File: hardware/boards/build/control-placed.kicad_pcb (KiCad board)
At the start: 4 copper layers, 177.9 x 107.5 mm, 106 parts

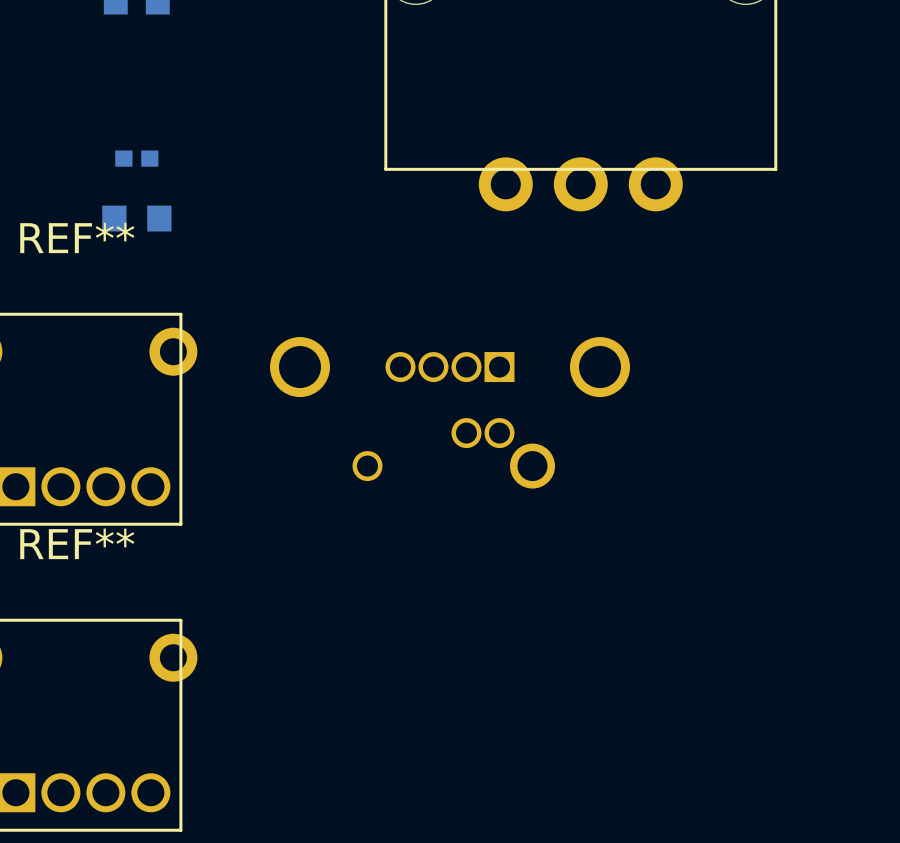
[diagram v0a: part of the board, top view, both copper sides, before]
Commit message: Move SD card slot from back to front of control board
The MicroSD slot needs to be accessible through the faceplate cutout,
so it must be on the front layer. Flipped footprint from B.Cu to F.Cu
in the KiCad PCB and added placement call in place_components.py to
position it at the faceplate cutout coordinates.

https://claude.ai/code/session_017d4oTDEiKrwHvNU6zuaWmu
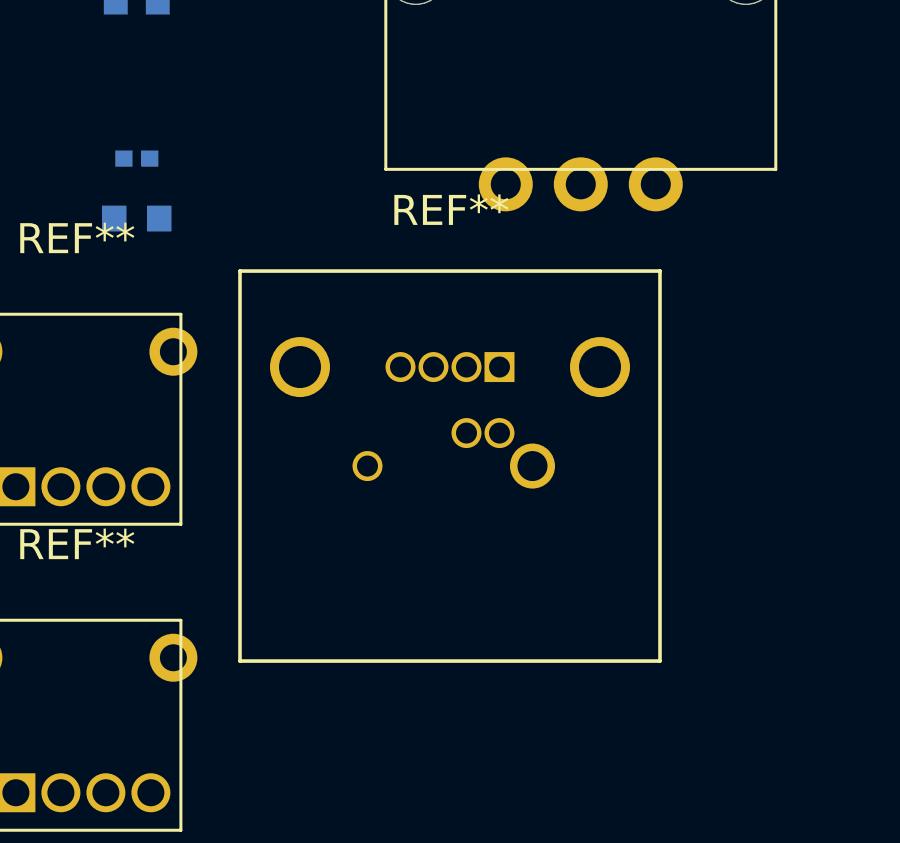
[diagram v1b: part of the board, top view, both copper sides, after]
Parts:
- REF**: moved to F.Cu
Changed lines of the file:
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@@
 	)
 	(footprint "PJS008U:PJS008U"
-		(layer "B.Cu")
+		(layer "F.Cu")
 		(at 100.94 90.25 180)
 		(property "Reference" "REF**"
 			(at 0 8.5 0)
-			(layer "B.SilkS")
+			(layer "F.SilkS")
 			(effects
 				(font
@@
 					(thickness 0.15)
 				)
-				(justify mirror)
 			)
 		)
 		(property "Value" "PJS008U"
 			(at 0 -8.5 0)
-			(layer "B.Fab")
+			(layer "F.Fab")
 			(effects
 				(font
@@
 					(thickness 0.15)
 				)
-				(justify mirror)
 			)
 		)
 		(property "Datasheet" ""
 			(at 0 0 0)
-			(layer "B.Fab")
+			(layer "F.Fab")
 			(hide yes)
 			(effects
@@
 					(thickness 0.15)
 				)
-				(justify mirror)
 			)
 		)
 		(property "Description" ""
 			(at 0 0 0)
-			(layer "B.Fab")
+			(layer "F.Fab")
 			(hide yes)
 			(effects
@@
 					(thickness 0.15)
 				)
-				(justify mirror)
 			)
 		)
@@
 				(type solid)
 			)
-			(layer "B.SilkS")
+			(layer "F.SilkS")
 		)
 		(fp_line
@@
 				(type solid)
 			)
-			(layer "B.SilkS")
+			(layer "F.SilkS")
 		)
 		(fp_line
@@
 				(type solid)
 			)
-			(layer "B.SilkS")
+			(layer "F.SilkS")
 		)
 		(fp_line
@@
 				(type solid)
 			)
-			(layer "B.SilkS")
+			(layer "F.SilkS")
 		)
 		(pad "" thru_hole circle

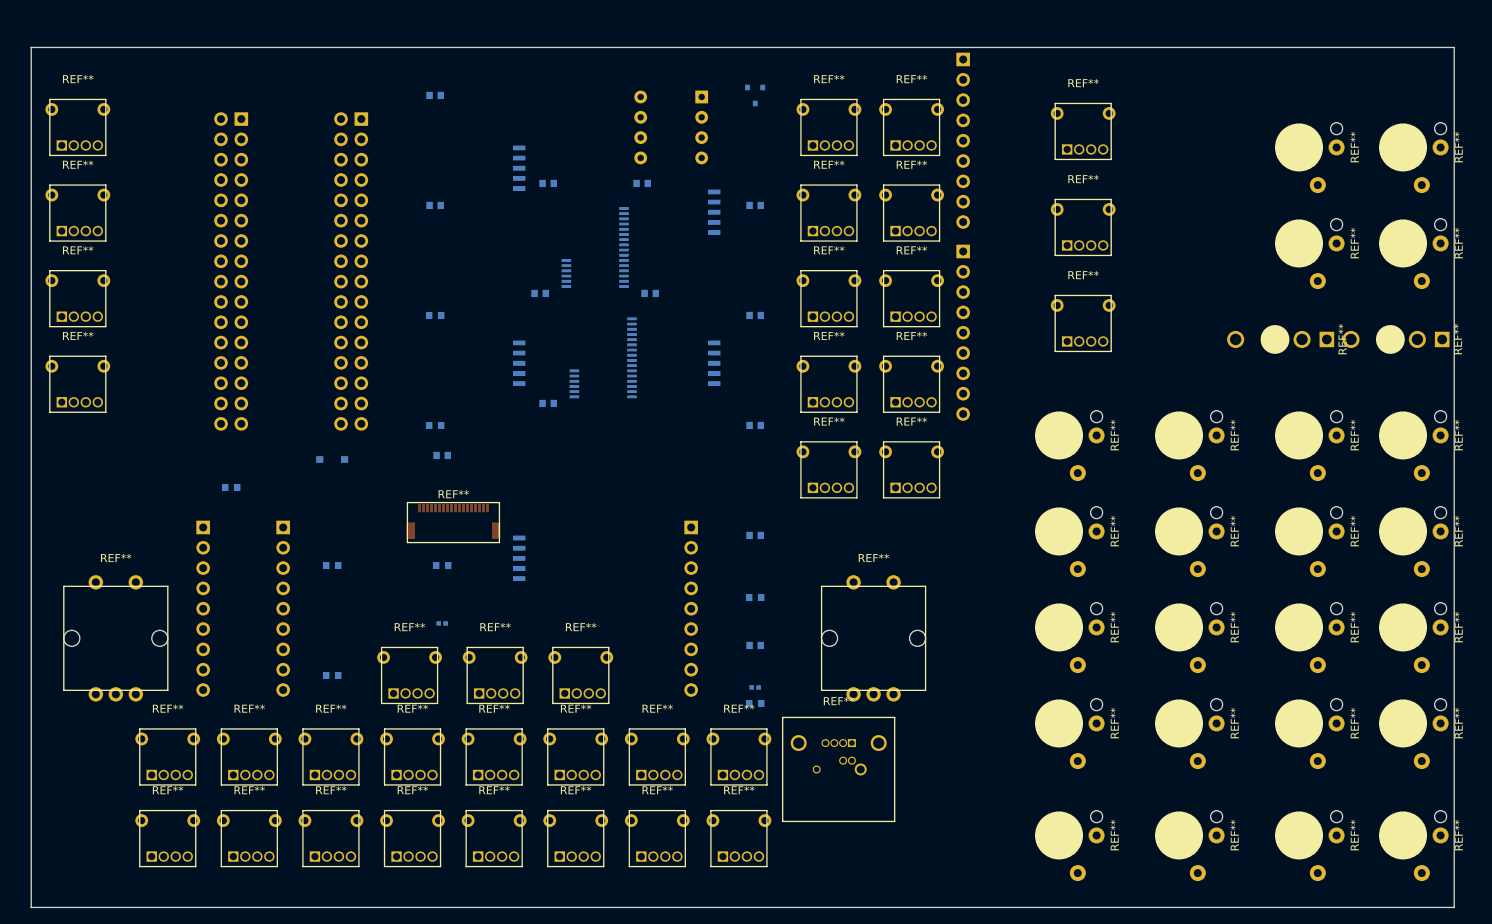
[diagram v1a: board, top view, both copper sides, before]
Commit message: Fix hardware pipeline: SD card position, faceplate holes, 3D assembly stack-up
- Fix SD card slot placement below PLAY button with component-map fallback
- Rebuild PJS008U 3D model as hollow card cage, align with faceplate cutout
- Inset USB-C connector flush with main board edge
- Add clock jack holes, SD cutout, JetBrains Mono fonts to faceplate
- Correct 3D assembly Z spacing from actual PJ398SM model measurements
- Improve explode animation: anchor control board, smoother slider
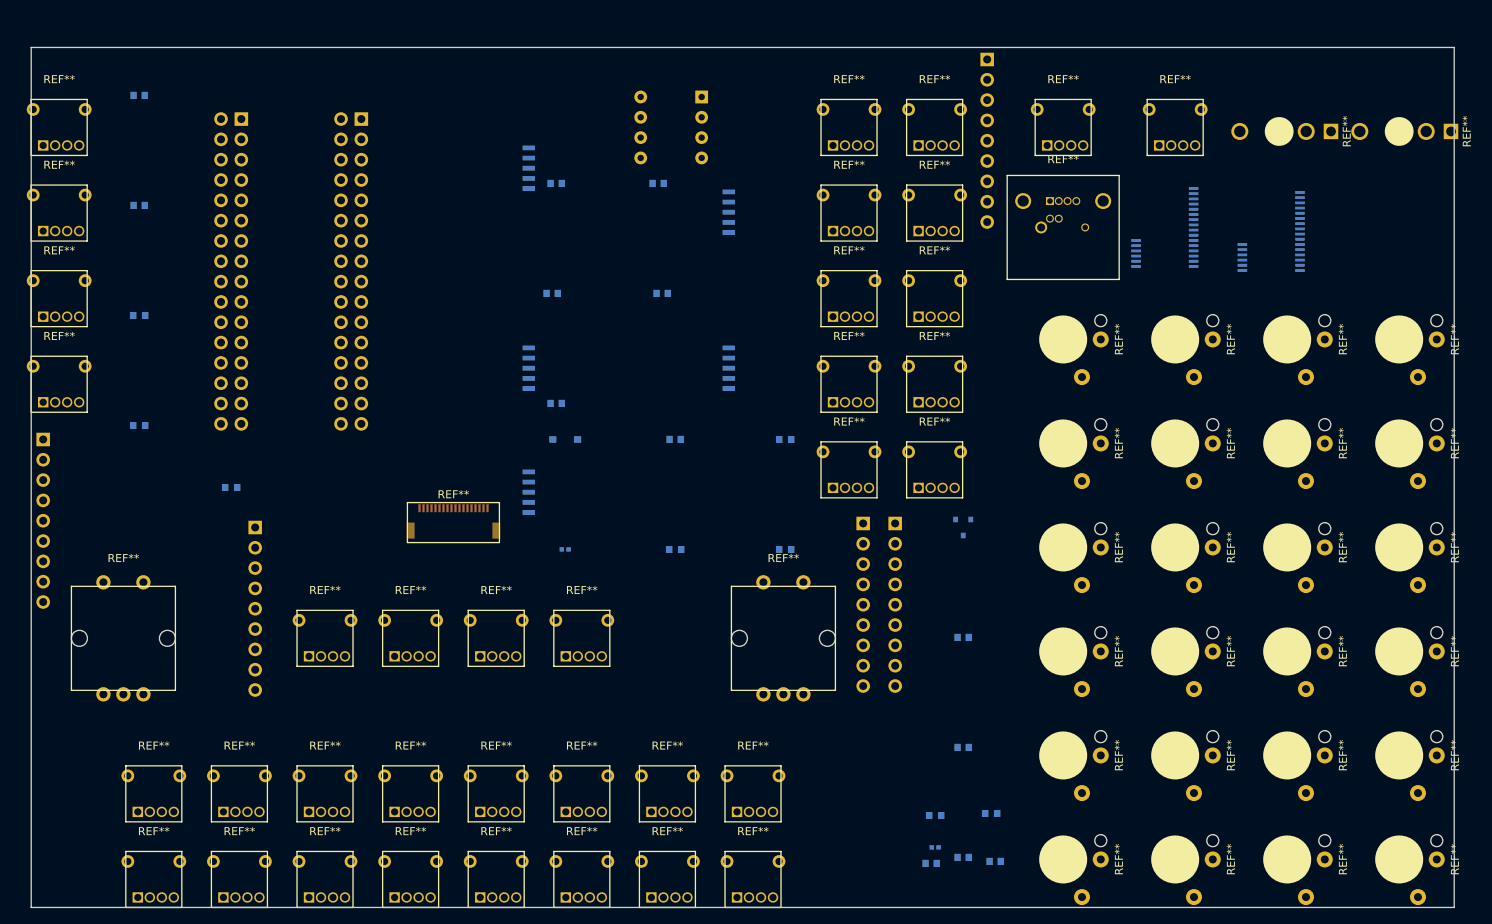
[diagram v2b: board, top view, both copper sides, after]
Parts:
- moved REF** 85.0 mm to (155.0, 23.0)
- moved REF** 74.0 mm to (68.8, 73.9)
- moved REF** 73.3 mm to (129.0, 22.5), turned to 0 degrees
- moved REF** 71.3 mm to (141.7, 22.5)
- moved C11 59.9 mm to (116.5, 101.2)
- moved C6 59.9 mm to (116.5, 87.5)
- moved C7 59.9 mm to (116.5, 73.8)
- moved REF** 59.9 mm to (116.5, 60.0)
- moved REF** 58.6 mm to (108.0, 59.5)
- moved R6 56.7 mm to (94.2, 62.8)
- moved REF** 49.0 mm to (157.0, 49.5)
- moved REF** 49.0 mm to (129.0, 49.5)
- moved REF** 49.0 mm to (143.0, 49.5)
- moved REF** 49.0 mm to (171.0, 49.5)
- moved C12 46.5 mm to (112.5, 102.0)
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
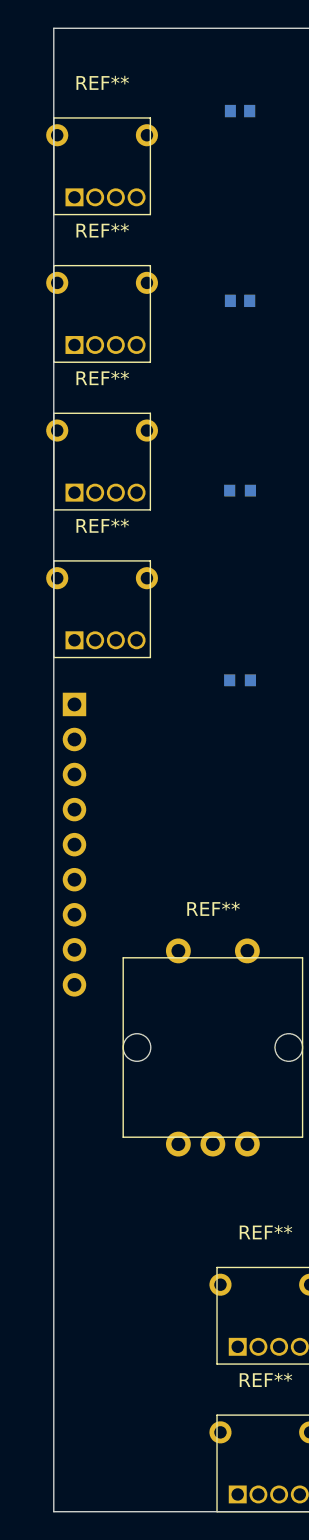
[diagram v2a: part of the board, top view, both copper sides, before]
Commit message: Throughhole m3 for stability
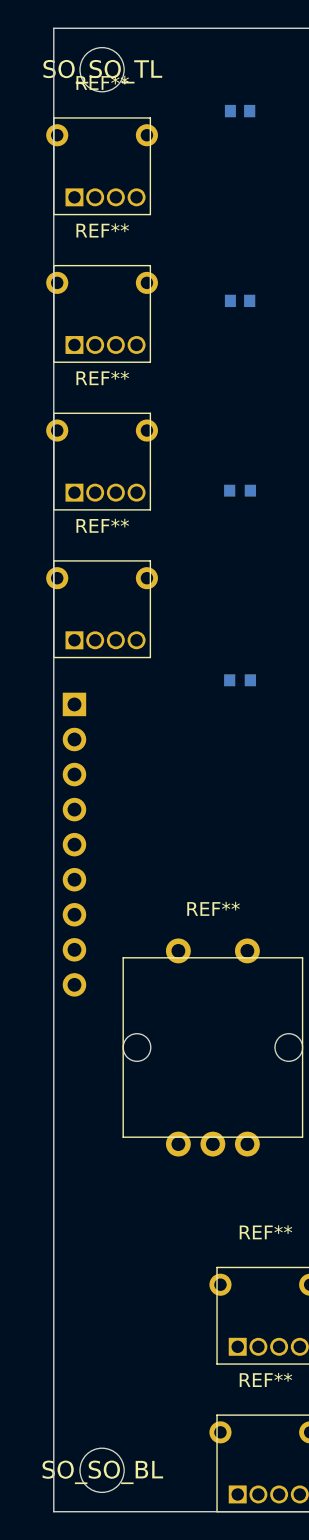
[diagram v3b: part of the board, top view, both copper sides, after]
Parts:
- added SO_SO_BL: M3_Standoff, , F.Cu at (3.50, 104.5)
- added SO_SO_TL: M3_Standoff, , F.Cu at (3.50, 3.00)
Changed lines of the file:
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@@
 		)
 	)
+	(footprint ""
+		(layer "F.Cu")
+		(at 3.5 3)
+		(property "Reference" "SO_SO_TL"
+			(at 0 0 0)
+			(layer "F.SilkS")
+			(effects
+				(font
+					(size 1.27 1.27)
+					(thickness 0.15)
+				)
+			)
+		)
+		(property "Value" "M3_Standoff"
+			(at 0 0 0)
+			(layer "F.Fab")
+			(effects
+				(font
+					(size 1.27 1.27)
+					(thickness 0.15)
+				)
+			)
+		)
+		(property "Datasheet" ""
+			(at 0 0 0)
+			(layer "F.Fab")
+			(hide yes)
+			(effects
+				(font
+					(size 1.27 1.27)
+					(thickness 0.15)
+				)
+			)
+		)
+		(property "Description" ""
+			(at 0 0 0)
+			(layer "F.Fab")
+			(hide yes)
+			(effects
+				(font
+					(size 1.27 1.27)
+					(thickness 0.15)
+				)
+			)
+		)
+		(attr exclude_from_pos_files exclude_from_bom)
+		(pad "" np_thru_hole circle
+			(at 0 0)
+			(size 3.2 3.2)
+			(drill 3.2)
+			(layers "*.Cu" "*.Mask")
+		)
+		(embedded_fonts no)
+	)
 	(footprint "PJ366ST:PJ366ST"
 		(layer "F.Cu")
@@
 		)
 	)
+	(footprint ""
+		(layer "F.Cu")
+		(at 3.5 104.5)
+		(property "Reference" "SO_SO_BL"
+			(at 0 0 0)
+			(layer "F.SilkS")
+			(effects
+				(font
+					(size 1.27 1.27)
+					(thickness 0.15)
+				)
+			)
+		)
+		(property "Value" "M3_Standoff"
+			(at 0 0 0)
+			(layer "F.Fab")
+			(effects
+				(font
+					(size 1.27 1.27)
+					(thickness 0.15)
+				)
+			)
+		)
+		(property "Datasheet" ""
+			(at 0 0 0)
+			(layer "F.Fab")
+			(hide yes)
+			(effects
+				(font
+					(size 1.27 1.27)
+					(thickness 0.15)
+				)
+			)
+		)
+		(property "Description" ""
+			(at 0 0 0)
+			(layer "F.Fab")
+			(hide yes)
+			(effects
+				(font
+					(size 1.27 1.27)
+					(thickness 0.15)
+				)
+			)
+		)
+		(attr exclude_from_pos_files exclude_from_bom)
+		(pad "" np_thru_hole circle
+			(at 0 0)
+			(size 3.2 3.2)
+			(drill 3.2)
+			(layers "*.Cu" "*.Mask")
+		)
+		(embedded_fonts no)
+	)
 	(footprint "PJ398SM:PJ398SM"
 		(layer "F.Cu")
@@
 	)
 	(gr_line
-		(start 177.88 0)
-		(end 177.88 107.5)
+		(start 0 107.5)
+		(end 0 0)
 		(stroke
 			(width 0.1)
@@
 	)
 	(gr_line
-		(start 177.88 107.5)
-		(end 0 107.5)
+		(start 177.88 0)
+		(end 177.88 107.5)
 		(stroke
 			(width 0.1)
@@
 	)
 	(gr_line
-		(start 0 107.5)
-		(end 0 0)
+		(start 177.88 107.5)
+		(end 0 107.5)
 		(stroke
 			(width 0.1)

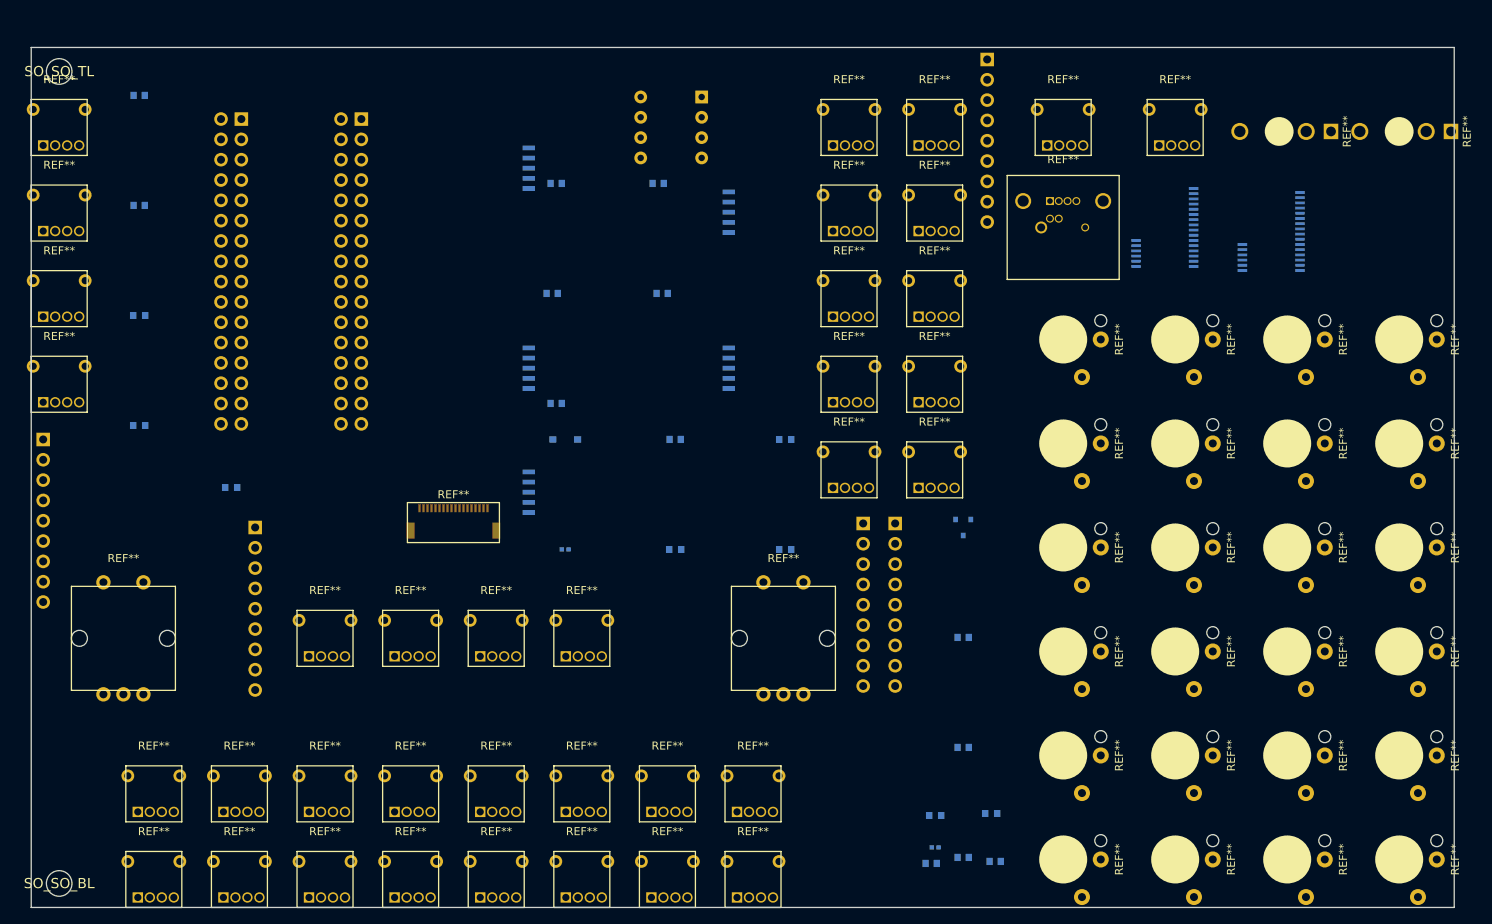
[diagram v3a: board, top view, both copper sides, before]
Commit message: Routing with design-rules.json
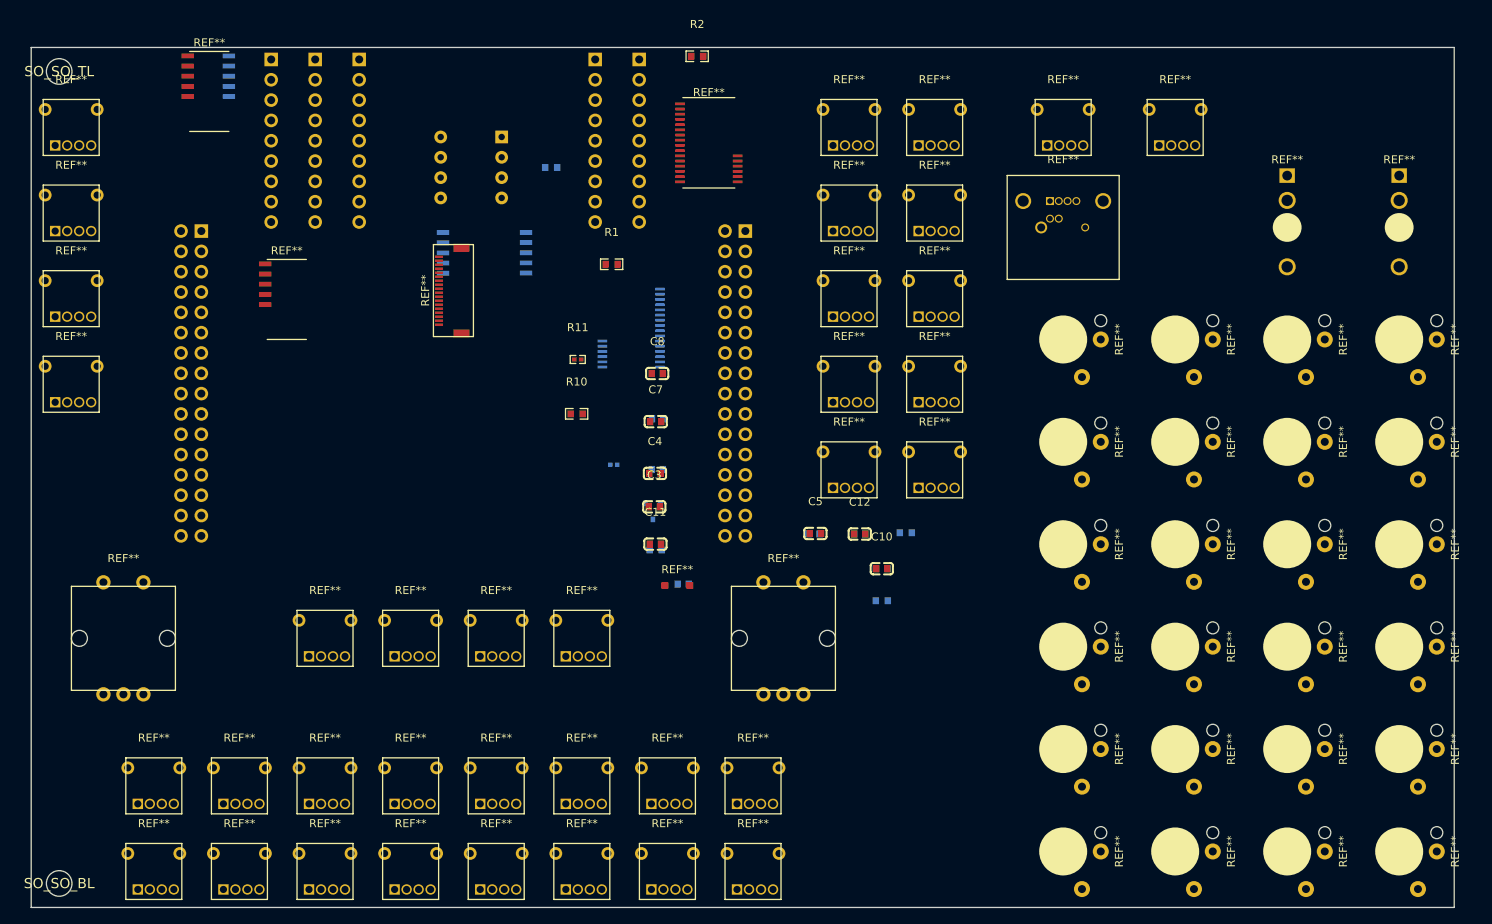
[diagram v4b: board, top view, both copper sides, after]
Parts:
- C10, C11, C12, C3, C4, C5, C7, C8, R1, R10, R11, R2, REF** (x4): moved to F.Cu
- moved C9 91.4 mm to (81.5, 67.1)
- moved REF** 85.6 mm to (41.0, 1.50)
- moved R2 83.6 mm to (83.2, 1.10), turned to 0 degrees
- moved R11 75.6 mm to (68.3, 39.0), turned to 0 degrees
- moved REF** 71.2 mm to (84.7, 11.9), turned to 0 degrees
- moved REF** 69.1 mm to (70.5, 1.50)
- moved C8 68.1 mm to (78.3, 40.8), turned to 0 degrees
- moved REF** 67.9 mm to (75.0, 35.1)
- moved R10 67.3 mm to (68.2, 45.8), turned to 0 degrees
- moved REF** 64.8 mm to (22.0, 5.50)
- moved R1 59.4 mm to (72.6, 27.1), turned to 0 degrees
- moved REF** 59.0 mm to (35.5, 1.50)
- moved R4 56.6 mm to (65.0, 15.0)
- moved C6 56.1 mm to (78.3, 46.4)
- moved REF** 55.4 mm to (30.0, 1.50)
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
